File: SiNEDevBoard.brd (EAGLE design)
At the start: 40 x 45 mm, 33 parts, among them IC1 ATTINY24/44/84-SSU, IC2 74HC164D, J1 AVR_SPI_PRG_6NS

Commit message: DevBoard v0.2
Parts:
- added JP1, JP2, JP3: FIDUCIAL1X2.5-STOP, CISECO eaglecad designs:FIDUCIAL-1X2.5-STOP
- added S1: (no value), CISECO eaglecad designs:TACTILE_SWITCH_SMD_LWK
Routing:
- net GND: track 4.72 -> 0.20 mm
- net VCC: track 11.0 -> 13.9 mm

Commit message: DevBoard V0.3
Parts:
- removed S1: (no value), CISECO eaglecad designs:TACTILE_SWITCH_SMD_LWK
- C1: value (none) -> 0603 100nF
- R1, R2: value (none) -> 0603 10K
- moved JP2 19.9 mm to (17.0, 29.7)
- moved JP1 7.68 mm to (7.00, 8.00)
- moved B2 3.16 mm to (7.67, 35.7)
- moved BAT1 3.16 mm to (20.0, 30.1)
- moved B1 3.16 mm to (7.67, 29.0)
- moved C1 1.41 mm to (7.93, 15.4)
- moved IC1 1.41 mm to (14.1, 20.8)
- moved IC2 1.41 mm to (26.0, 27.6)
- moved J1 1.41 mm to (14.1, 10.8)
- moved JP3 1.41 mm to (34.6, 4.33)
- moved LED1 1.41 mm to (32.1, 17.9)
- moved LED10 1.41 mm to (21.9, 12.8)
- moved LED11 1.41 mm to (32.1, 7.76)
- moved LED12 1.41 mm to (29.5, 7.76)
- moved LED13 1.41 mm to (27.0, 7.76)
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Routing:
- net BTN2: track 22.9 -> 20.9 mm
- net BTN1: track 13.4 -> 11.4 mm
- net GND: track 0.20 -> 2.07 mm
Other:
- board size 40 x 45 mm -> 38 x 40 mm
- board text added: "EMWave 2013"
- board text added: "SiNE DevBoard"
- board text added: "v0.3"

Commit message: DevBoard V0.4
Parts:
- removed U$1: IRRECEIVERSMD, SparkFun:TSOP8523
- added TP1: TPB2,54, CISECO eaglecad designs:B2,54
- added U$2: IR-RECEIVER, CISECO eaglecad designs:TSOP35X
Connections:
- removed net N$2: IC1.5
- new net TESTPAD: IC1.5, TP1.TP
- net GND: now also U$2.1, U$2.2; no longer U$1.1, U$1.4, U$1.5
- net N$6: now also U$2.4; no longer U$1.3
- net VCC: now also U$2.3; no longer U$1.2
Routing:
- net TESTPAD: track 0.00 -> 6.13 mm
- net N$6: track 4.39 -> 3.36 mm
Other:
- board size 38 x 40 mm -> 40 x 42 mm
- board text added: "v0.4"
- board text removed: "v0.3"

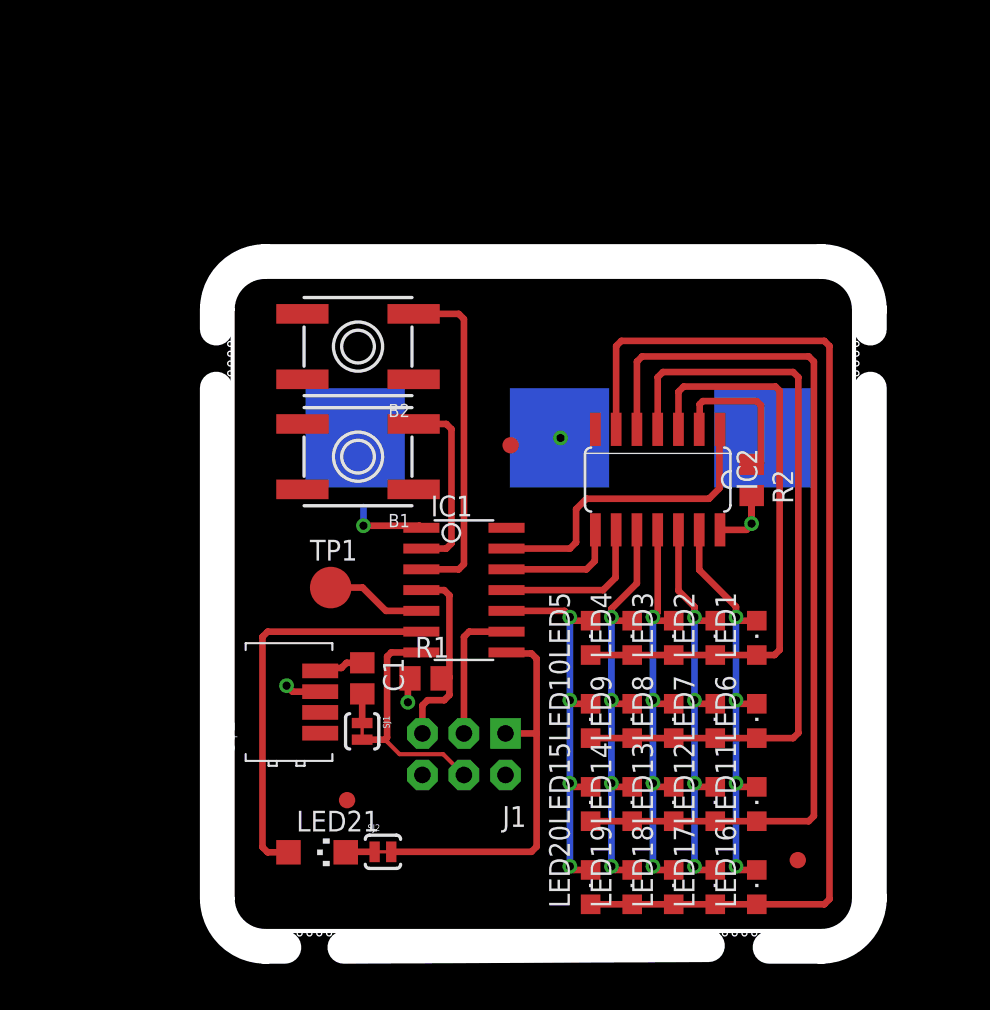
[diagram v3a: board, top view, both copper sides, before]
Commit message: DevBoard V0.5 Final Changes including Teardrops, this version was sent to make 3 prototype boards
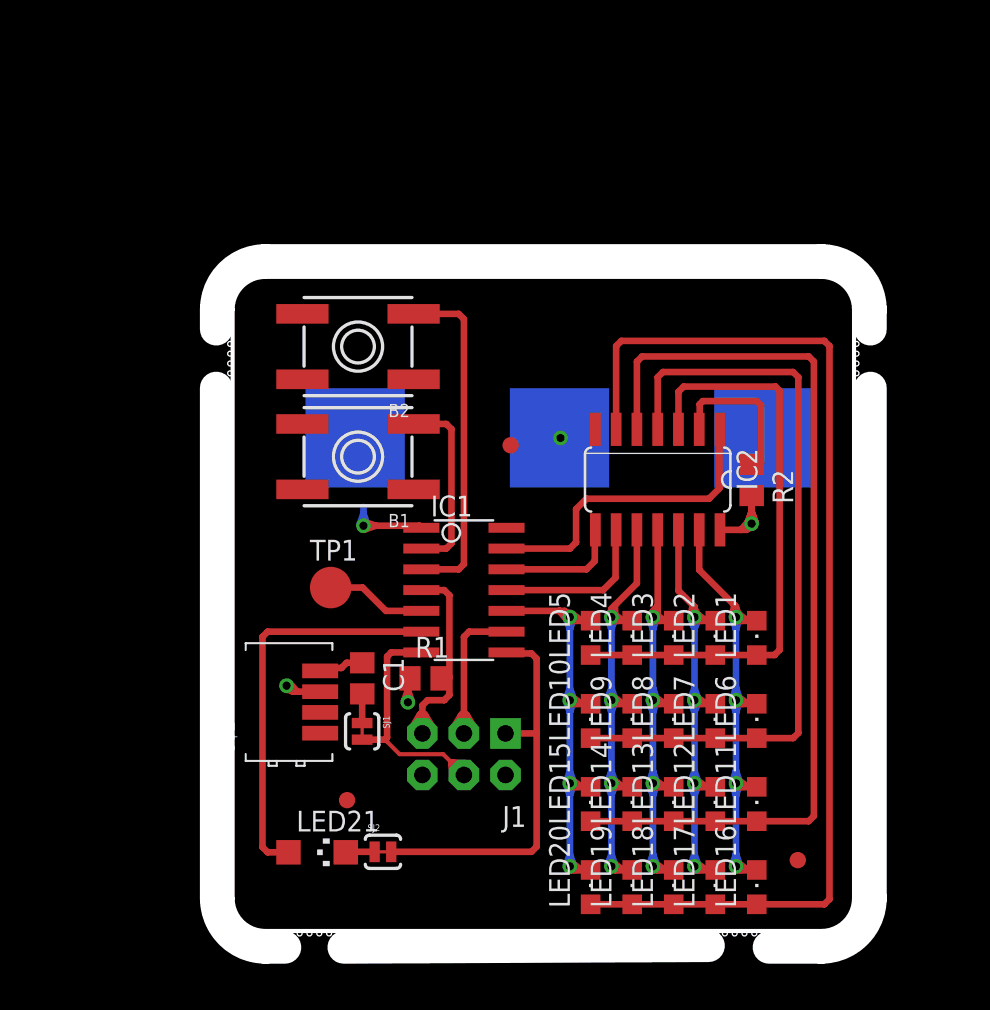
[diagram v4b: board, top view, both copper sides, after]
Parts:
- B1: value (none) -> SWICTH_SMD
- B2: value (none) -> SWITCH_SMD
- LED1, LED10, LED11, LED12, LED13, LED14, LED15, LED16, LED17, LED18, LED19, LED2, LED20, LED3, LED4, LED5, LED6, LED7, LED8, LED9: value (none) -> 0805 LED
- LED21: value (none) -> IR_SENDER
- SJ1, SJ2: value SOLDERJUMPERTRACE -> SOLDERJUMPERTRACE (NP)
- TP1: value TPB2,54 -> TPB2,54(NP)
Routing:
- net LED_C4: track 26.7 -> 47.7 mm
- net LED_C3: track 26.1 -> 47.2 mm
- net LED_C2: track 26.4 -> 47.5 mm
- net LED_C1: track 27.0 -> 48.0 mm
- net LED_C5: track 24.8 -> 45.8 mm
- net VCC: track 14.6 -> 28.0 mm
- net MOSI: track 14.5 -> 17.4 mm
- net SCK: track 8.64 -> 11.4 mm
- net RESET: track 12.1 -> 14.9 mm
- net GND: track 2.07 -> 3.99 mm
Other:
- board text added: "v0.5"
- board text removed: "v0.4"

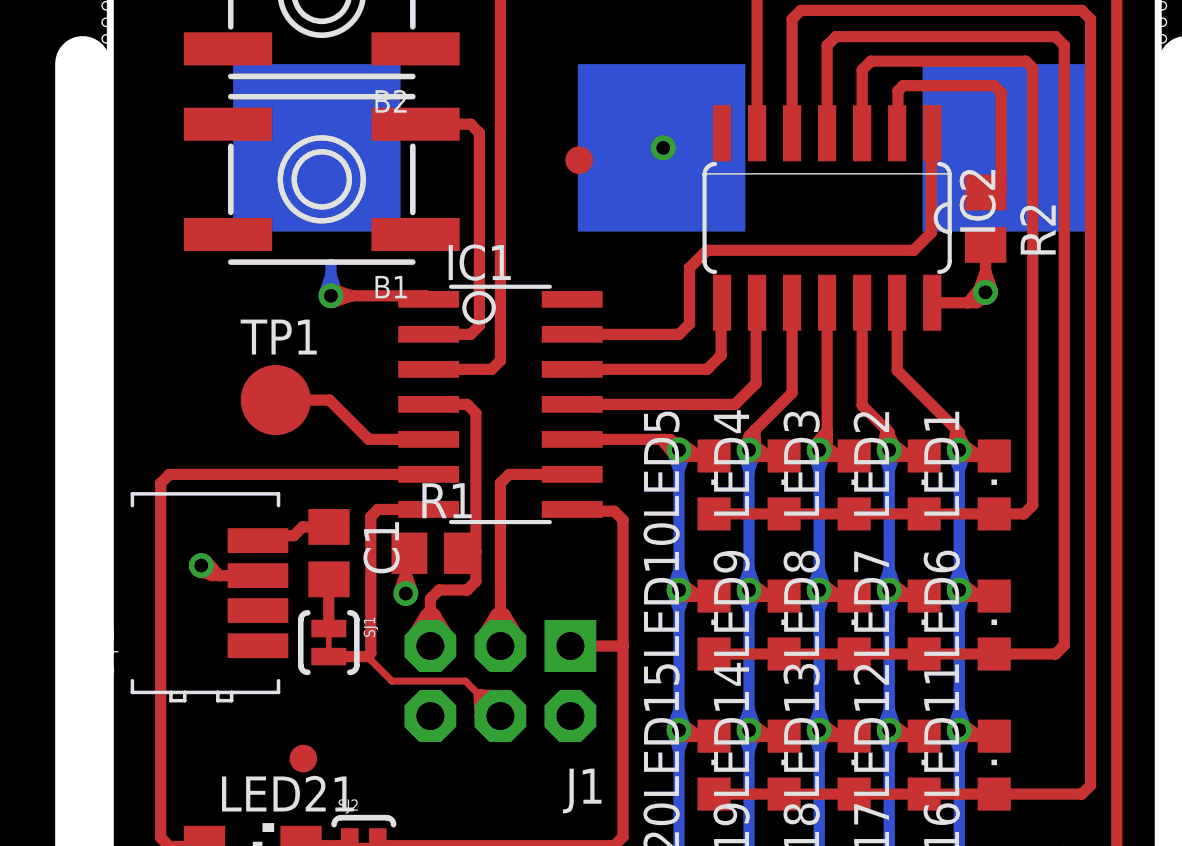
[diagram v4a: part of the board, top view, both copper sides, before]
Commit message: Added parts use in DevBoard v0.5 to the lbr Update parts in the DevBoard to use versions from the lbr DevBoard V0.5a
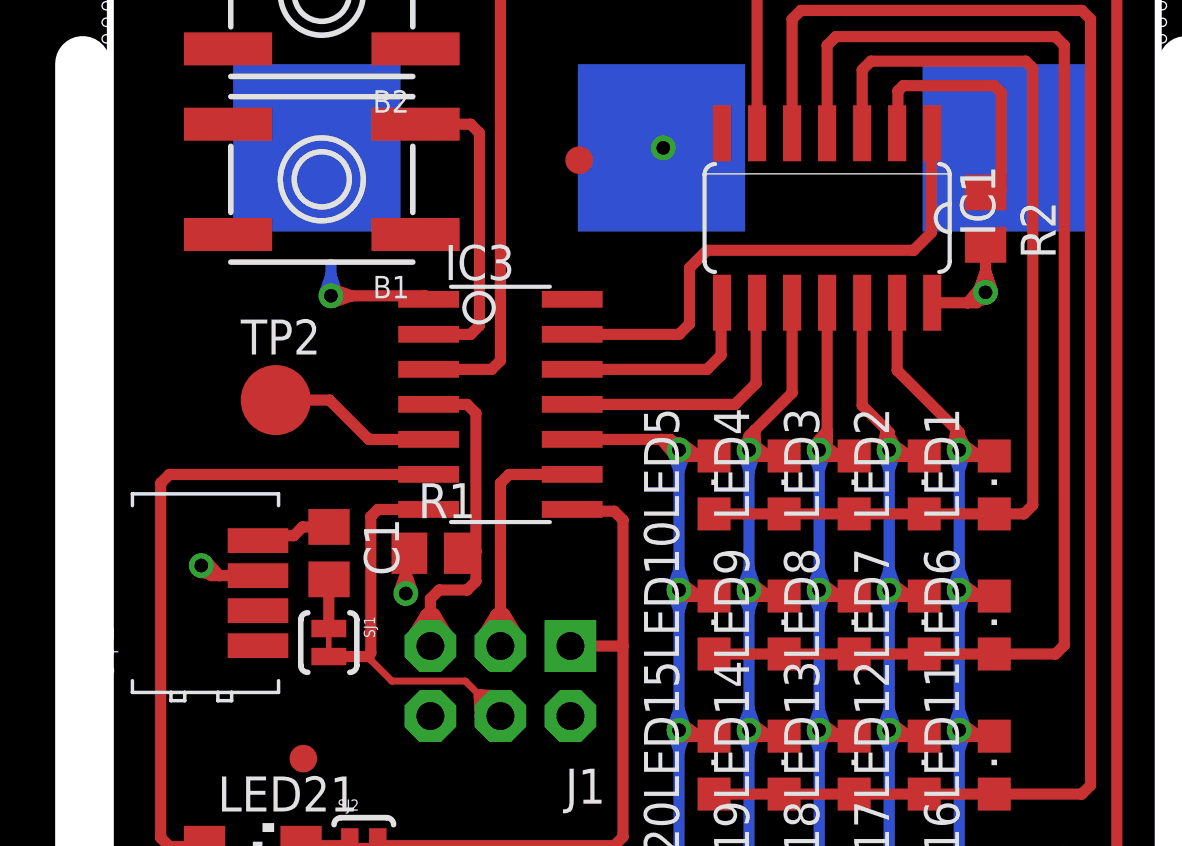
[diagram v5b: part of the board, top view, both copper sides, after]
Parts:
- removed BAT1: (no value), SparkFun:BATTCON_20MM
- removed IC2: 74HC164D, 74xx-eu:SO14
- removed TP1: TPB2,54(NP), CISECO eaglecad designs:B2,54
- removed U$2: IR-RECEIVER, CISECO eaglecad designs:TSOP35X
- added BAT2: (no value), SiNE Parts:BATTCON_20MM
- added IC3: ATTINY24/44/84-SSU, SiNE Parts:SOIC14
- added TP2: TPB2,54, SiNE Parts:B2,54
- added U$1: IR-RECEIVER, SiNE Parts:TSOP35X
- IC1: value ATTINY24/44/84-SSU -> 74HCT164D; device attiny24_44_84:SOIC14 -> SiNE Parts:SO14
- LED1, LED10, LED11, LED12, LED13, LED14, LED15, LED16, LED17, LED18, LED19, LED2, LED20, LED3, LED4, LED5, LED6, LED7, LED8, LED9: device adafruit:CHIPLED_0805 -> adafruit:CHIPLED_0805@1
- LED21: device led:CHIPLED_1206 -> led:CHIPLED_1206@1
- moved IC1 13.6 mm to (26.0, 27.6), turned to 180 degrees
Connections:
- net BTN1: now also IC3.2; no longer IC1.2
- net BTN2: now also IC3.3; no longer IC1.3
- net GND: now also BAT2.2, IC1.7, IC3.14, U$1.1, U$1.2; no longer BAT1.2, IC1.14, IC2.7, U$2.1, U$2.2
- net IR_PWM: now also IC3.6; no longer IC1.6
- net LED_C1: now also IC1.13; no longer IC2.13
- net LED_C2: now also IC1.12; no longer IC2.12
- net LED_C3: now also IC1.11; no longer IC2.11
- net LED_C4: now also IC1.10; no longer IC2.10
- net LED_C5: now also IC3.10; no longer IC1.10
- net LED_R1: now also IC1.3; no longer IC2.3
- net LED_R2: now also IC1.4; no longer IC2.4
- net LED_R3: now also IC1.5; no longer IC2.5
- net LED_R4: now also IC1.6; no longer IC2.6
- net MISO: now also IC3.8; no longer IC1.8
- net MOSI: now also IC3.7; no longer IC1.7
- net N$1: now also IC1.2; no longer IC2.2
- net N$6: now also U$1.4; no longer U$2.4
- net RESET: now also IC3.4; no longer IC1.4
- net SCK: now also IC3.9; no longer IC1.9
- net SR_A: now also IC1.1, IC3.13; no longer IC1.13, IC2.1
- net SR_CLK: now also IC1.8, IC3.12; no longer IC1.12, IC2.8
- net SR_CLR: now also IC1.9, IC3.11; no longer IC1.11, IC2.9
- net TESTPAD: now also IC3.5, TP2.TP; no longer IC1.5, TP1.TP
- net VCC: now also BAT2.1, IC1.14, IC3.1, U$1.3; no longer BAT1.1, IC1.1, IC2.14, U$2.3
